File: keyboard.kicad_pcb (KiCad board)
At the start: 2 copper layers, 168 parts, among them J1 SSD1306, J3 USB_C_Receptacle_USB2.0, SW10 MX_SW_HS, SW11 MX_SW_HS, SW12 MX_SW_HS, SW13 MX_SW_HS, SW14 MX_SW_HS, SW15 MX_SW_HS, SW16 MX_SW_HS, SW17 MX_SW_HS, SW18 MX_SW_HS, SW19 MX_SW_HS, SW20 MX_SW_HS, SW21 MX_SW_HS, SW22 MX_SW_HS, SW23 MX_SW_HS, SW24 MX_SW_HS, SW25 MX_SW_HS, SW26 MX_SW_HS, SW27 MX_SW_HS, SW28 MX_SW_HS, SW29 MX_SW_HS, SW30 MX_SW_HS, SW31 MX_SW_HS, SW32 MX_SW_HS, SW33 MX_SW_HS, SW34 MX_SW_HS, SW35 MX_SW_HS, SW36 MX_SW_HS, SW37 MX_SW_HS, SW38 MX_SW_HS, SW39 MX_SW_HS, SW4 MX_SW_HS, SW40 MX_SW_HS, SW41 MX_SW_HS, SW42 MX_SW_HS, SW43 MX_SW_HS, SW44 MX_SW_HS, SW45 MX_SW_HS, SW46 MX_SW_HS, SW47 MX_SW_HS, SW48 MX_SW_HS, SW49 MX_SW_HS, SW5 MX_SW_HS, SW50 MX_SW_HS, SW51 MX_SW_HS, SW52 MX_SW_HS, SW53 MX_SW_HS, SW54 MX_SW_HS, SW55 MX_SW_HS, SW56 MX_SW_HS, SW57 MX_SW_HS, SW58 MX_SW_HS, SW59 MX_SW_HS, SW6 MX_SW_HS, SW60 MX_SW_HS, SW61 MX_SW_HS, SW62 MX_SW_HS, SW63 MX_SW_HS, SW64 MX_SW_HS, SW65 MX_SW_HS, SW66 MX_SW_HS, SW67 MX_SW_HS, SW68 MX_SW_HS, SW69 MX_SW_HS, SW7 MX_SW_HS, SW70 MX_SW_HS, SW71 MX_SW_HS, SW8 MX_SW_HS, SW9 MX_SW_HS, U2 AMS1117-3.3, U3 SRV05-4

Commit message: changed layout, started routing
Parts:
- D1, D10, D11, D12, D13, D14, D15, D16, D17, D18, D19, D2, D20, D21, D22, D23, D24, D25, D26, D27, D28, D29, D3, D30, D31, D32, D33, D34, D35, D36, D37, D38, D39, D4, D40, D41, D42, D43, D44, D45, D46, D47, D48, D49, D5, D50, D51, D52, D53, D54, D55, D56, D57, D58, D59, D6, D60, D61, D62, D63, D64, D65, D66, D67, D68, D7, D8, D9: footprint Diode_THT:D_DO-35_SOD27_P5.08mm_Horizontal -> marbastvary:D_DO-35_SOD27_P5.08mm_Horizontal
- SW1: renamed from ROTARY SWITCH
- moved SW1 280.4 mm to (311.1, 72.5)
- moved C_VDDIO1 184.8 mm to (58.4, 78.5), turned to -90 degrees
- moved C_VDDIO2 165.9 mm to (85.1, 80.0), turned to 90 degrees
- moved C1 154.4 mm to (39.4, 78.5), turned to -90 degrees
- moved C2 153.1 mm to (45.7, 78.5), turned to -90 degrees
- moved C_VDD3 151.9 mm to (71.1, 78.5), turned to -90 degrees
- moved C_VDDA2 151.4 mm to (64.8, 78.5), turned to -90 degrees
- moved U3 146.1 mm to (29.2, 59.7)
- moved R5 142.4 mm to (34.3, 69.8)
- moved C_VDD2 140.7 mm to (95.2, 80.0), turned to 90 degrees
- moved C_VDD1 139.4 mm to (90.2, 80.0), turned to 90 degrees
- moved R3 136.1 mm to (31.8, 69.8), turned to 180 degrees
- moved J2 135.1 mm to (58.4, 58.4)
- moved C_VDDA1 131.7 mm to (77.5, 78.5), turned to -90 degrees
- moved R7 126.8 mm to (49.5, 69.8)
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- renumbered POWER to D69, SWD to J2, BOOT to SW2, RESET to SW3, STM32 to U1
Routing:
- net col0: track 0.00 -> 290.8 mm, vias 0 -> 2
- net ENC_SW: track 0.00 -> 260.8 mm
- net ENC_B: track 0.00 -> 260.3 mm, vias 0 -> 2
- net ENC_A: track 0.00 -> 250.5 mm, vias 0 -> 2
- net I2C_SCL: track 0.00 -> 203.2 mm
- net I2C_SDA: track 0.00 -> 202.5 mm
- net Net-(D1-A): track 0.00 -> 97.1 mm, vias 0 -> 2
- net col1: track 0.00 -> 94.2 mm
- net col6: track 0.00 -> 93.0 mm
- net col13: track 5.39 -> 98.1 mm
- net col2: track 0.00 -> 92.4 mm
- net col9: track 0.00 -> 89.4 mm
- net col10: track 0.00 -> 89.0 mm
- net col12: track 0.00 -> 86.6 mm
- net Net-(D2-A): track 0.00 -> 84.4 mm, vias 0 -> 2
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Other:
- board outline added: 315 x 134.6 mm

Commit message: more wiring done
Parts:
- moved R5 27.9 mm to (62.2, 69.8), turned to 180 degrees
- moved R7 10.2 mm to (39.4, 69.8), turned to 180 degrees
- moved R6 7.62 mm to (49.5, 69.8)
- moved C1 1.73 mm to (39.4, 80.2), turned to 90 degrees
- moved C2 1.73 mm to (45.7, 80.2), turned to 90 degrees
- moved C_VDD3 1.73 mm to (71.1, 80.2), turned to 90 degrees
- moved C_VDDA1 1.50 mm to (77.5, 80.0), turned to 90 degrees
- moved C_VDDA2 1.50 mm to (64.8, 80.0), turned to 90 degrees
- moved C_VDDIO1 1.50 mm to (58.4, 80.0), turned to 90 degrees
- moved C_VDD2 1.27 mm to (94.0, 80.0)
- moved C_VDDIO2 1.27 mm to (83.8, 80.0)
- moved C_VDD1 1.27 mm to (88.9, 80.0)
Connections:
- U1 pad 10: row0 -> row2
- U1 pad 12: row2 -> row0
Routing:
- net Net-(D60-A): track 0.00 -> 298.0 mm, vias 0 -> 6
- net Net-(D31-A): track 0.00 -> 275.9 mm, vias 0 -> 7
- net Net-(D61-A): track 0.00 -> 274.3 mm, vias 0 -> 2
- net Net-(D32-A): track 0.00 -> 266.5 mm, vias 0 -> 7
- net row2: track 0.00 -> 239.1 mm, vias 0 -> 2
- net GND: track 0.00 -> 225.9 mm
- net Net-(D45-A): track 0.00 -> 216.6 mm, vias 0 -> 6
- net Net-(D46-A): track 0.00 -> 181.6 mm, vias 0 -> 2
- net row4: track 0.00 -> 176.1 mm, vias 0 -> 2
- net Net-(D17-A): track 0.00 -> 160.7 mm, vias 0 -> 9
- net row1: track 0.00 -> 158.7 mm, vias 0 -> 4
- net row3: track 0.00 -> 139.3 mm, vias 0 -> 2
- net +3.3V: track 6.35 -> 118.7 mm
- net row0: track 0.00 -> 103.5 mm
- net +5V: track 0.00 -> 82.4 mm, vias 0 -> 3
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
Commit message: nuked traces, start again
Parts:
- moved C_VDD1 2.77 mm to (87.6, 77.5), turned to -90 degrees
- moved C_VDD2 2.77 mm to (92.7, 77.5), turned to -90 degrees
- moved C_VDDIO2 2.77 mm to (82.5, 77.5), turned to -90 degrees
- moved C_VDD3 2.15 mm to (69.8, 78.5), turned to -90 degrees
- moved C1 2.15 mm to (38.1, 78.5), turned to -90 degrees
- moved C2 2.15 mm to (44.5, 78.5), turned to -90 degrees
- moved C_VDDIO1 1.97 mm to (57.1, 78.5), turned to -90 degrees
- moved C_VDDA1 1.97 mm to (76.2, 78.5), turned to -90 degrees
- moved C_VDDA2 1.97 mm to (63.5, 78.5), turned to -90 degrees
- moved C3 1.80 mm to (50.8, 78.7), turned to -90 degrees
- turned S2 to 180 degrees
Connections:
- J1 pad 3: +3V3 -> +3.3V
- J2 pad 1: +3V3 -> +3.3V
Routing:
- net Net-(D60-A): track 298.0 -> 0.00 mm, vias 6 -> 0
- net Net-(D31-A): track 275.9 -> 0.00 mm, vias 7 -> 0
- net Net-(D61-A): track 274.3 -> 0.00 mm, vias 2 -> 0
- net Net-(D32-A): track 266.5 -> 0.00 mm, vias 7 -> 0
- net +3.3V: track 118.7 -> 369.6 mm, vias 0 -> 4
- net Net-(D56-A): track 3.18 -> 224.0 mm
- net Net-(D45-A): track 216.6 -> 0.00 mm, vias 6 -> 0
- net col0: track 289.8 -> 85.1 mm, vias 2 -> 0
- net Net-(D46-A): track 181.6 -> 0.00 mm, vias 2 -> 0
- net Net-(D17-A): track 160.7 -> 0.00 mm, vias 9 -> 0
- net Net-(D1-A): track 97.1 -> 0.00 mm, vias 2 -> 0
- net Net-(D2-A): track 85.1 -> 0.00 mm, vias 2 -> 0
- net SWCLK: track 0.00 -> 69.5 mm, vias 0 -> 2
- net Net-(D16-A): track 61.1 -> 0.00 mm, vias 3 -> 0
- net +5V: track 82.4 -> 28.6 mm, vias 3 -> 0
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
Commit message: added more traces
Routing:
- net BOOT0: track 24.4 -> 45.6 mm, vias 0 -> 3
- net +5V: track 28.6 -> 49.0 mm, vias 0 -> 2

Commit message: more traces done
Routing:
- net Net-(D15-A): track 0.00 -> 187.7 mm, vias 0 -> 1
- net Net-(D14-A): track 0.00 -> 161.3 mm, vias 0 -> 2
- net Net-(D13-A): track 0.00 -> 135.0 mm, vias 0 -> 1
- net Net-(D12-A): track 0.00 -> 124.9 mm, vias 0 -> 2
- net Net-(D11-A): track 0.00 -> 98.5 mm, vias 0 -> 2
- net Net-(D1-A): track 0.00 -> 96.3 mm, vias 0 -> 2
- net Net-(D2-A): track 0.00 -> 90.5 mm, vias 0 -> 4
- net Net-(D10-A): track 0.00 -> 83.6 mm, vias 0 -> 1
- net Net-(D3-A): track 0.00 -> 71.5 mm, vias 0 -> 2
- net Net-(D5-A): track 0.00 -> 63.8 mm, vias 0 -> 2
- net Net-(D9-A): track 0.00 -> 62.9 mm, vias 0 -> 2
- net Net-(D4-A): track 0.00 -> 56.0 mm, vias 0 -> 2
- net Net-(D8-A): track 0.00 -> 44.9 mm, vias 0 -> 2
- net Net-(D6-A): track 0.00 -> 40.4 mm, vias 0 -> 2
- net Net-(D7-A): track 0.00 -> 33.3 mm, vias 0 -> 2
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
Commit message: added more traces
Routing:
- net Net-(D31-A): track 0.00 -> 291.7 mm, vias 0 -> 4
- net Net-(D32-A): track 0.00 -> 281.1 mm, vias 0 -> 4
- net Net-(D34-A): track 0.00 -> 263.0 mm, vias 0 -> 4
- net Net-(D33-A): track 0.00 -> 256.1 mm, vias 0 -> 5
- net Net-(D35-A): track 0.00 -> 235.6 mm, vias 0 -> 4
- net Net-(D56-A): track 224.0 -> 0.00 mm
- net Net-(D16-A): track 0.00 -> 172.3 mm, vias 0 -> 4
- net Net-(D17-A): track 0.00 -> 149.6 mm, vias 0 -> 3
- net Net-(D30-A): track 0.00 -> 148.5 mm, vias 0 -> 2
- net Net-(D18-A): track 0.00 -> 138.1 mm, vias 0 -> 4
- net Net-(D29-A): track 0.00 -> 126.9 mm, vias 0 -> 2
- net Net-(D19-A): track 0.00 -> 116.8 mm, vias 0 -> 3
- net Net-(D20-A): track 0.00 -> 109.0 mm, vias 0 -> 4
- net Net-(D28-A): track 0.00 -> 108.2 mm, vias 0 -> 2
- net Net-(D38-A): track 0.00 -> 104.1 mm, vias 0 -> 6
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
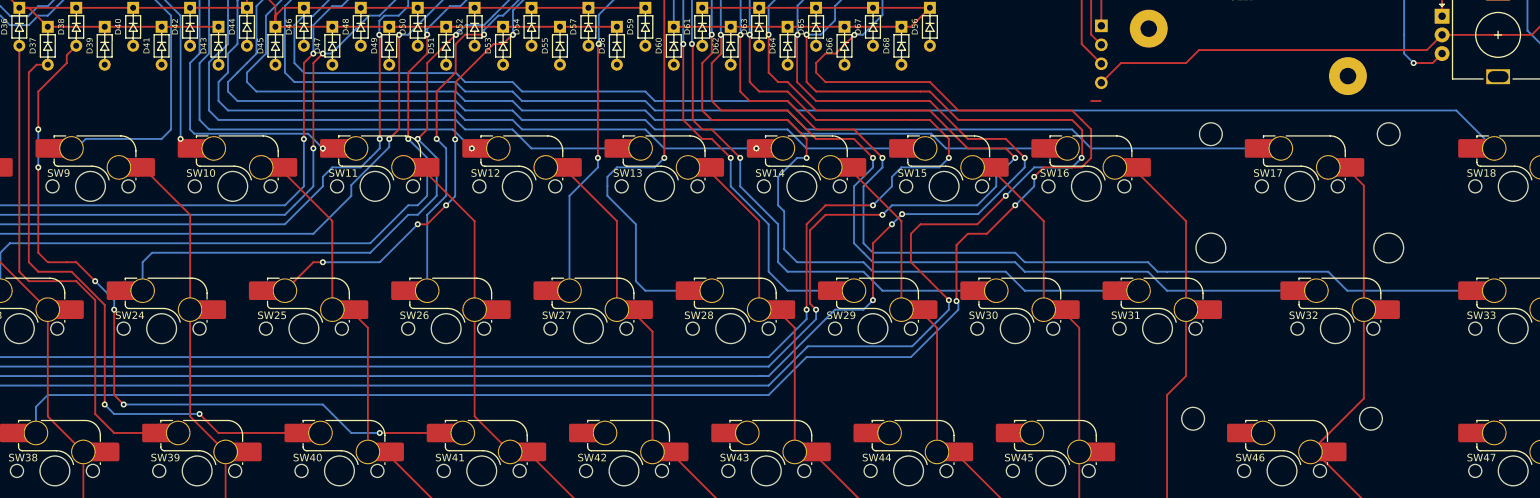
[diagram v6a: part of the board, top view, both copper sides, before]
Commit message: added more traces
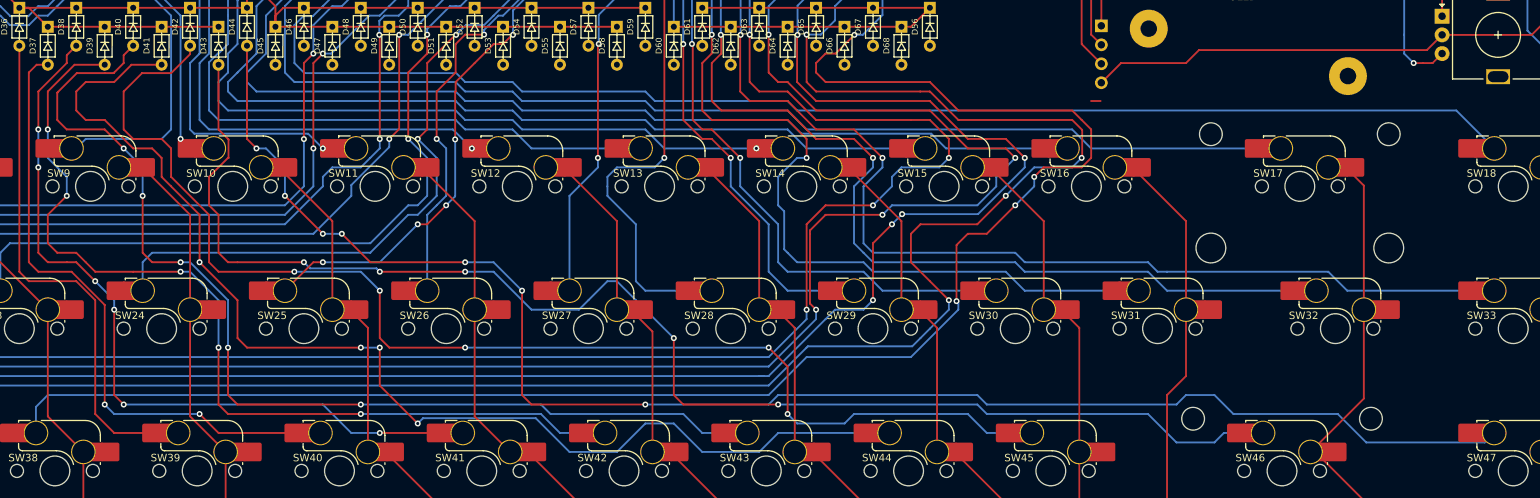
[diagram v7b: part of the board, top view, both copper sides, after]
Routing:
- net Net-(D44-A): track 0.00 -> 209.4 mm, vias 0 -> 7
- net Net-(D43-A): track 0.00 -> 185.9 mm, vias 0 -> 5
- net Net-(D42-A): track 0.00 -> 170.1 mm, vias 0 -> 5
- net Net-(D41-A): track 0.00 -> 159.2 mm, vias 0 -> 4
- net Net-(D40-A): track 0.00 -> 140.9 mm, vias 0 -> 5
- net Net-(D39-A): track 0.00 -> 124.8 mm, vias 0 -> 5

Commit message: code?
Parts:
- removed C_VDD1, C_VDD2, C_VDDIO2: 100n, Capacitor_THT:C_Disc_D5.0mm_W2.5mm_P2.50mm
- removed C_VDD3, C_VDDIO1: 4.7u, Capacitor_THT:CP_Radial_D4.0mm_P1.50mm
- removed C_VDDA1: 10u, Capacitor_THT:CP_Radial_D4.0mm_P1.50mm
- removed C_VDDA2: 1u, Capacitor_THT:CP_Radial_D4.0mm_P1.50mm
- removed F1: 500mA, marbastvary:polyfuse_5.1mm
- removed R2, R3, R4: 5.1k, Resistor_THT:R_Axial_DIN0204_L3.6mm_D1.6mm_P5.08mm_Horizontal
- removed R5: 68, Resistor_THT:R_Axial_DIN0204_L3.6mm_D1.6mm_P5.08mm_Horizontal
- removed R7: 1k, Resistor_THT:R_Axial_DIN0204_L3.6mm_D1.6mm_P5.08mm_Horizontal
- removed SW1: RotaryEncoder_Switch, Rotary_Encoder:RotaryEncoder_Alps_EC11E-Switch_Vertical_H20mm
- removed SW2: SW_Push, Button_Switch_THT:SW_PUSH_6mm
- added C10: 1u, Capacitor_SMD:C_0805_2012Metric, F.Cu at (220.2, 86.6)
- added C11: 1u, Capacitor_SMD:C_0805_2012Metric, F.Cu at (120.5, 79.0)
- added C4: 4.7u, Capacitor_SMD:C_0805_2012Metric, F.Cu at (206.0, 78.2)
- added C5: 100n, Capacitor_SMD:C_0603_1608Metric, F.Cu at (208.0, 80.1)
- added C6: 4.7u, Capacitor_SMD:C_0805_2012Metric, F.Cu at (213.2, 89.2)
- added C7: 100n, Capacitor_SMD:C_0603_1608Metric, F.Cu at (216.7, 88.8)
- added C8: 100n, Capacitor_SMD:C_0603_1608Metric, F.Cu at (216.4, 74.7)
- added C9: 10u, Capacitor_SMD:C_0805_2012Metric, F.Cu at (222.2, 88.4)
- added D70: D, marbastvary:D_DO-35_SOD27_P5.08mm_Horizontal, F.Cu at (215.1, 70.1)
- added D71: D, marbastvary:D_DO-35_SOD27_P5.08mm_Horizontal, F.Cu at (215.4, 70.1)
- added H1: MountingHole_Pad, MountingHole:MountingHole_3.2mm_M3_Pad, F.Cu at (55.0, 192.0)
- added H2: MountingHole_Pad, MountingHole:MountingHole_3.2mm_M3_Pad, F.Cu at (375.0, 192.0)
- added H3: MountingHole_Pad, MountingHole:MountingHole_3.2mm_M3_Pad, F.Cu at (375.0, 62.0)
- added H4: MountingHole_Pad, MountingHole:MountingHole_3.2mm_M3_Pad, F.Cu at (55.0, 62.0)
- added J4: Conn_01x02_Male, Connector_PinHeader_2.54mm:PinHeader_1x02_P2.54mm_Vertical, F.Cu at (110.5, 69.5)
- added R8: 5.1k, Resistor_THT:R_Axial_DIN0207_L6.3mm_D2.5mm_P7.62mm_Horizontal, F.Cu at (222.8, 58.7)
- C1, C2: value 10uF -> 100n; footprint Capacitor_THT:CP_Radial_D4.0mm_P1.50mm -> Capacitor_SMD:C_0805_2012Metric
- C3: value 1u -> 10u; footprint Capacitor_THT:CP_Radial_D4.0mm_P1.50mm -> Capacitor_SMD:C_0805_2012Metric
- D1: value D -> LED; footprint marbastvary:D_DO-35_SOD27_P5.08mm_Horizontal -> LED_THT:LED_D3.0mm_Clear
- D69: value LED -> D; footprint LED_THT:LED_D3.0mm_Clear -> marbastvary:D_DO-35_SOD27_P5.08mm_Horizontal
- J1: value SSD1306 -> Conn_02x05_Odd_Even; footprint marbastvary:SSD1306 -> Connector:322010010000
- J2: value Conn_01x05 -> USB_C_Receptacle_USB2.0; footprint Connector_PinHeader_2.54mm:PinHeader_1x05_P2.54mm_Vertical -> Connector_USB:USB_C_Receptacle_G-Switch_GT-USB-7010ASV
- J3: value USB_C_Receptacle_USB2.0 -> SSD1306; footprint USB-C:TYPE-C-31-M-12 -> marbastvary:SSD1306
- R1: value 5.1k -> 100R; footprint Resistor_THT:R_Axial_DIN0204_L3.6mm_D1.6mm_P5.08mm_Horizontal -> Resistor_THT:R_Axial_DIN0207_L6.3mm_D2.5mm_P7.62mm_Horizontal
- R6: value 68 -> 5.1k; footprint Resistor_THT:R_Axial_DIN0204_L3.6mm_D1.6mm_P5.08mm_Horizontal -> Resistor_THT:R_Axial_DIN0207_L6.3mm_D2.5mm_P7.62mm_Horizontal
- SW10, SW11, SW12, SW13, SW14, SW15, SW16, SW17, SW18, SW20, SW21, SW22, SW23, SW24, SW25, SW26, SW27, SW28, SW29, SW30, SW31, SW33, SW35, SW36, SW37, SW38, SW39, SW4, SW40, SW41, SW42, SW43, SW44, SW45, SW46, SW47, SW48, SW49, SW5, SW50, SW51, SW52, SW53, SW54, SW55, SW56, SW57, SW58, SW6, SW61, SW66, SW67, SW68, SW69, SW7, SW70, SW71, SW8, SW9: footprint marbastmx:SW_MX_HS_1u -> marbastmx:SW_MX_1u
- SW19, SW32: footprint marbastmx:SW_MX_HS_1.5u -> marbastmx:SW_MX_1.5u
- SW3: value SW_Push -> RotaryEncoder_Switch; footprint Button_Switch_THT:SW_PUSH_6mm -> Rotary_Encoder:RotaryEncoder_Alps_EC11E-Switch_Vertical_H20mm
- SW34: footprint marbastmx:SW_MX_HS_1.75u -> marbastmx:SW_MX_1.75u
- SW59: footprint marbastmx:SW_MX_HS_1u -> marbastmx:SW_MX_1.75u
- SW60: footprint marbastmx:SW_MX_HS_1.75u -> marbastmx:SW_MX_1u
- SW62: footprint marbastmx:SW_MX_HS_1u -> marbastmx:SW_MX_1.25u
- SW63, SW64: footprint marbastmx:SW_MX_HS_1.25u -> marbastmx:SW_MX_1.25u
- SW65: footprint marbastmx:SW_MX_HS_1.25u -> marbastmx:SW_MX_1u
- U1: value STM32F072CBTx -> LM2937xT; footprint Package_QFP:LQFP-48_7x7mm_P0.5mm -> Package_TO_SOT_THT:TO-220-3_Horizontal_TabDown
- U2: value AMS1117-3.3 -> L9110; footprint Package_TO_SOT_SMD:SOT-223-3_TabPin2 -> Package_DIP:DIP-8_W7.62mm
- U3: value SRV05-4 -> STM32F072CBTx; footprint marbastvary:SOT-23-6-routable -> Package_QFP:LQFP-48_7x7mm_P0.5mm
- moved SW3 273.1 mm to (354.8, 72.8), turned to -90 degrees
- moved SW62 246.4 mm to (76.0, 182.1)
- moved D69 220.5 mm to (293.8, 87.9), turned to -90 degrees
- moved U3 187.1 mm to (215.0, 81.9), turned to 135 degrees
- moved C3 182.4 mm to (232.4, 95.2), turned to 180 degrees
- moved C2 180.2 mm to (224.0, 93.3)
- moved R6 176.3 mm to (225.8, 66.3), turned to 90 degrees
- moved J2 156.9 mm to (215.3, 61.3), turned to 180 degrees
- moved U1 134.2 mm to (228.3, 92.3), turned to 0 degrees
- moved R1 133.7 mm to (203.5, 66.3), turned to 90 degrees
- moved D40 119.9 mm to (254.4, 87.9)
- moved D39 119.8 mm to (251.1, 86.3)
- moved D42 118.9 mm to (261.0, 87.9)
- moved D41 118.8 mm to (257.7, 86.3)
- moved D44 117.9 mm to (267.6, 87.9)
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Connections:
- C1 pad 1: +5V -> /VBUS
- C2 pad 1: +3.3V -> /VBUS
- C3 pad 1: NRST -> +3.3V
- D1 pad 1: row0 -> Net-(D1-K)
- D1 pad 2: Net-(D1-A) -> /VBUS
- D16 pad 1: row1 -> row0
- D31 pad 1: row2 -> row1
- D45 pad 1: row3 -> row2
- D56 pad 1: row4 -> row3
- D69 pad 1: Net-(D69-K) -> row4
- D69 pad 2: +5V -> Net-(D69-A)
- J1 pad 1: I2C_SDA -> +3.3V
- J1 pad 2: I2C_SCL -> SWDIO
- J1 pad 3: +3.3V -> GND
- J1 pad 4: GND -> SWCLK
- J1 pad 5: unconnected-(J1-MNT-Pad5) -> GND
- R1 pad 1: GND -> Net-(D1-K)
- R1 pad 2: BOOT0 -> GND
- R6 pad 1: Net-(U1-PA12) -> Net-(J2-CC1)
- R6 pad 2: D_P -> GND
- SW10 pad 2: Net-(D7-A) -> Net-(D8-A)
- SW11 pad 2: Net-(D8-A) -> Net-(D9-A)
- SW12 pad 2: Net-(D9-A) -> Net-(D10-A)
- SW13 pad 2: Net-(D10-A) -> Net-(D11-A)
- SW14 pad 2: Net-(D11-A) -> Net-(D12-A)
- SW15 pad 2: Net-(D12-A) -> Net-(D13-A)
- SW16 pad 2: Net-(D13-A) -> Net-(D14-A)
- SW17 pad 2: Net-(D14-A) -> Net-(D15-A)
- SW18 pad 2: Net-(D15-A) -> Net-(D16-A)
- SW19 pad 2: Net-(D16-A) -> Net-(D17-A)
- SW20 pad 2: Net-(D17-A) -> Net-(D18-A)
- SW21 pad 2: Net-(D18-A) -> Net-(D19-A)
- SW22 pad 2: Net-(D19-A) -> Net-(D20-A)
- SW23 pad 2: Net-(D20-A) -> Net-(D21-A)
- SW24 pad 2: Net-(D21-A) -> Net-(D22-A)
- SW25 pad 2: Net-(D22-A) -> Net-(D23-A)
- SW26 pad 2: Net-(D23-A) -> Net-(D24-A)
- SW27 pad 2: Net-(D24-A) -> Net-(D25-A)
- SW28 pad 2: Net-(D25-A) -> Net-(D26-A)
- SW29 pad 2: Net-(D26-A) -> Net-(D27-A)
- SW30 pad 2: Net-(D27-A) -> Net-(D28-A)
- SW31 pad 2: Net-(D28-A) -> Net-(D29-A)
- SW32 pad 2: Net-(D29-A) -> Net-(D30-A)
- SW33 pad 2: Net-(D30-A) -> Net-(D31-A)
- SW34 pad 2: Net-(D31-A) -> Net-(D32-A)
- SW35 pad 2: Net-(D32-A) -> Net-(D33-A)
- SW36 pad 2: Net-(D33-A) -> Net-(D34-A)
- SW37 pad 2: Net-(D34-A) -> Net-(D35-A)
- SW38 pad 2: Net-(D35-A) -> Net-(D36-A)
- SW39 pad 2: Net-(D36-A) -> Net-(D37-A)
- SW4 pad 2: Net-(D1-A) -> Net-(D2-A)
- SW40 pad 2: Net-(D37-A) -> Net-(D38-A)
- SW41 pad 2: Net-(D38-A) -> Net-(D39-A)
- SW42 pad 2: Net-(D39-A) -> Net-(D40-A)
- SW43 pad 2: Net-(D40-A) -> Net-(D41-A)
- SW44 pad 2: Net-(D41-A) -> Net-(D42-A)
- SW45 pad 2: Net-(D42-A) -> Net-(D43-A)
- SW46 pad 2: Net-(D43-A) -> Net-(D44-A)
- SW47 pad 2: Net-(D44-A) -> Net-(D45-A)
- SW48 pad 2: Net-(D45-A) -> Net-(D46-A)
- SW49 pad 2: Net-(D46-A) -> Net-(D47-A)
- SW5 pad 2: Net-(D2-A) -> Net-(D3-A)
- SW50 pad 2: Net-(D47-A) -> Net-(D48-A)
- SW51 pad 2: Net-(D48-A) -> Net-(D49-A)
- SW52 pad 2: Net-(D49-A) -> Net-(D50-A)
- SW53 pad 2: Net-(D50-A) -> Net-(D51-A)
- SW54 pad 2: Net-(D51-A) -> Net-(D52-A)
- SW55 pad 2: Net-(D52-A) -> Net-(D53-A)
- SW56 pad 2: Net-(D53-A) -> Net-(D54-A)
- SW57 pad 2: Net-(D54-A) -> Net-(D55-A)
- SW58 pad 2: Net-(D55-A) -> Net-(D56-A)
- SW59 pad 1: col14 -> col12
- SW59 pad 2: Net-(D56-A) -> Net-(D57-A)
- SW6 pad 2: Net-(D3-A) -> Net-(D4-A)
- SW60 pad 1: col12 -> col13
- SW60 pad 2: Net-(D57-A) -> Net-(D58-A)
- SW61 pad 1: col13 -> col14
- SW61 pad 2: Net-(D58-A) -> Net-(D59-A)
- SW62 pad 1: col14 -> col0
- SW62 pad 2: Net-(D59-A) -> Net-(D60-A)
- SW63 pad 1: col0 -> col1
- SW63 pad 2: Net-(D60-A) -> Net-(D61-A)
- SW64 pad 1: col1 -> col2
- SW64 pad 2: Net-(D61-A) -> Net-(D62-A)
- SW65 pad 1: col2 -> col6
- SW65 pad 2: Net-(D62-A) -> Net-(D63-A)
- SW66 pad 1: col6 -> col9
- SW66 pad 2: Net-(D63-A) -> Net-(D64-A)
- SW67 pad 1: col9 -> col10
- SW67 pad 2: Net-(D64-A) -> Net-(D65-A)
- SW68 pad 1: col10 -> col11
- SW68 pad 2: Net-(D65-A) -> Net-(D66-A)
- SW69 pad 1: col11 -> col12
- SW69 pad 2: Net-(D66-A) -> Net-(D67-A)
- SW7 pad 2: Net-(D4-A) -> Net-(D5-A)
- SW70 pad 1: col12 -> col13
- SW70 pad 2: Net-(D67-A) -> Net-(D68-A)
- SW71 pad 1: col13 -> col14
- SW71 pad 2: Net-(D68-A) -> Net-(D69-A)
- SW8 pad 2: Net-(D5-A) -> Net-(D6-A)
- SW9 pad 2: Net-(D6-A) -> Net-(D7-A)
- U1 pad 1: +3.3V -> /VBUS
- U1 pad 2: unconnected-(U1-PC13-Pad2) -> GND
- U1 pad 3: unconnected-(U1-PC14-Pad3) -> +3.3V
- U2 pad 1: GND -> Net-(J4-Pin_2)
- U2 pad 2: +3.3V -> /VBUS
- U2 pad 3: +5V -> /VBUS
- U3 pad 1: D_P -> +3.3V
- U3 pad 2: GND -> /FWD
- U3 pad 3: unconnected-(U3-IO2-Pad3) -> /REV
- U3 pad 5: +5V -> unconnected-(U3-PF0-Pad5)
- U3 pad 6: D_N -> unconnected-(U3-PF1-Pad6)
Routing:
- net Net-(D62-A): track 0.00 -> 361.1 mm
- net Net-(D48-A): track 0.00 -> 346.0 mm
- net Net-(D63-A): track 0.00 -> 344.1 mm
- net Net-(D61-A): track 0.00 -> 342.0 mm
- net Net-(D47-A): track 0.00 -> 329.0 mm
- net Net-(D60-A): track 0.00 -> 321.8 mm
- net Net-(D46-A): track 0.00 -> 303.1 mm
- net Net-(D64-A): track 0.00 -> 274.0 mm
- net Net-(D65-A): track 0.00 -> 253.3 mm, vias 0 -> 1
- net Net-(D66-A): track 0.00 -> 233.4 mm, vias 0 -> 2
- net GND: track 229.3 -> 0.00 mm, vias 2 -> 266
- net Net-(D59-A): track 0.00 -> 229.0 mm, vias 0 -> 2
- net Net-(D67-A): track 0.00 -> 210.6 mm, vias 0 -> 1
- net Net-(D58-A): track 0.00 -> 205.6 mm, vias 0 -> 2
- net Net-(D68-A): track 0.00 -> 190.5 mm, vias 0 -> 1
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- added copper zone on F.Cu, net +3.3V
- added copper zone on B.Cu, net /VBUS
- added copper zone on F.Cu, net /VBUS
- added copper zone on B.Cu, net GND
- added copper zone on F.Cu, net GND
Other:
- board size 315 x 134.6 mm -> 330 x 140 mm
- board text added: "JLCJLCJLC"
- board text removed: "OLED"
